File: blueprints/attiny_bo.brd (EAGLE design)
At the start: 36 x 20 mm, 8 parts, among them IC1 ATTiny85, J1 AVR_SPI_PRG_6NS

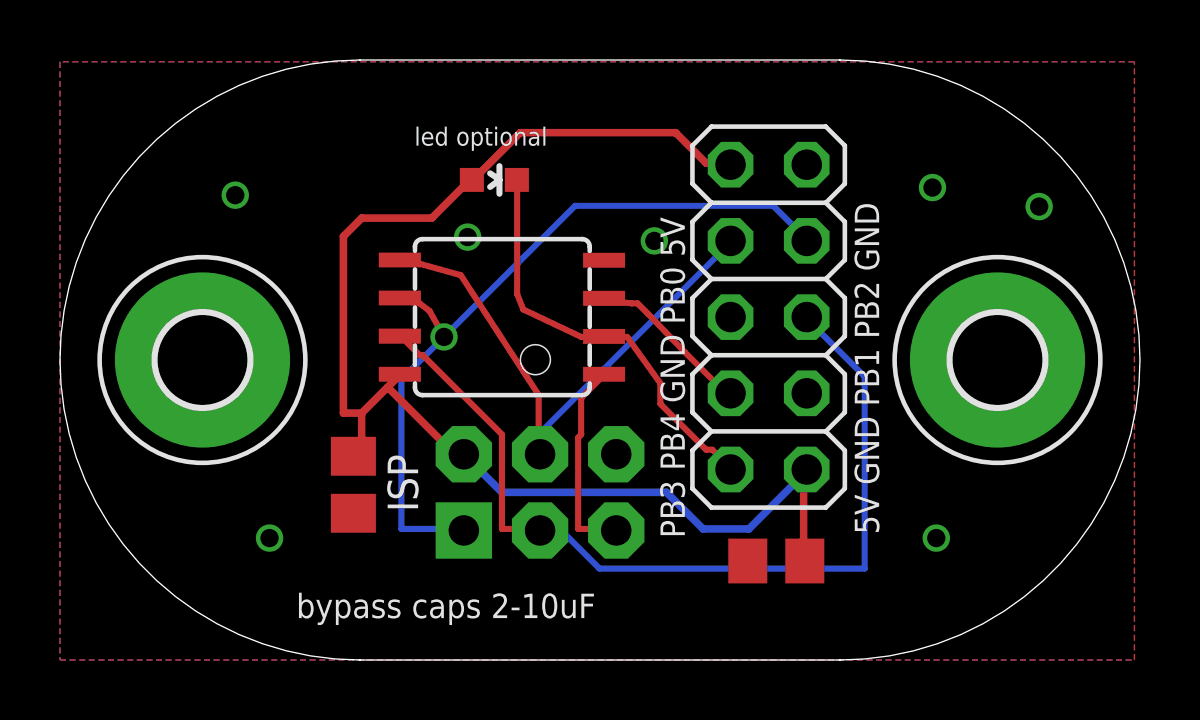
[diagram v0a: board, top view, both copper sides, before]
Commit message: started adding optional crystal to the board
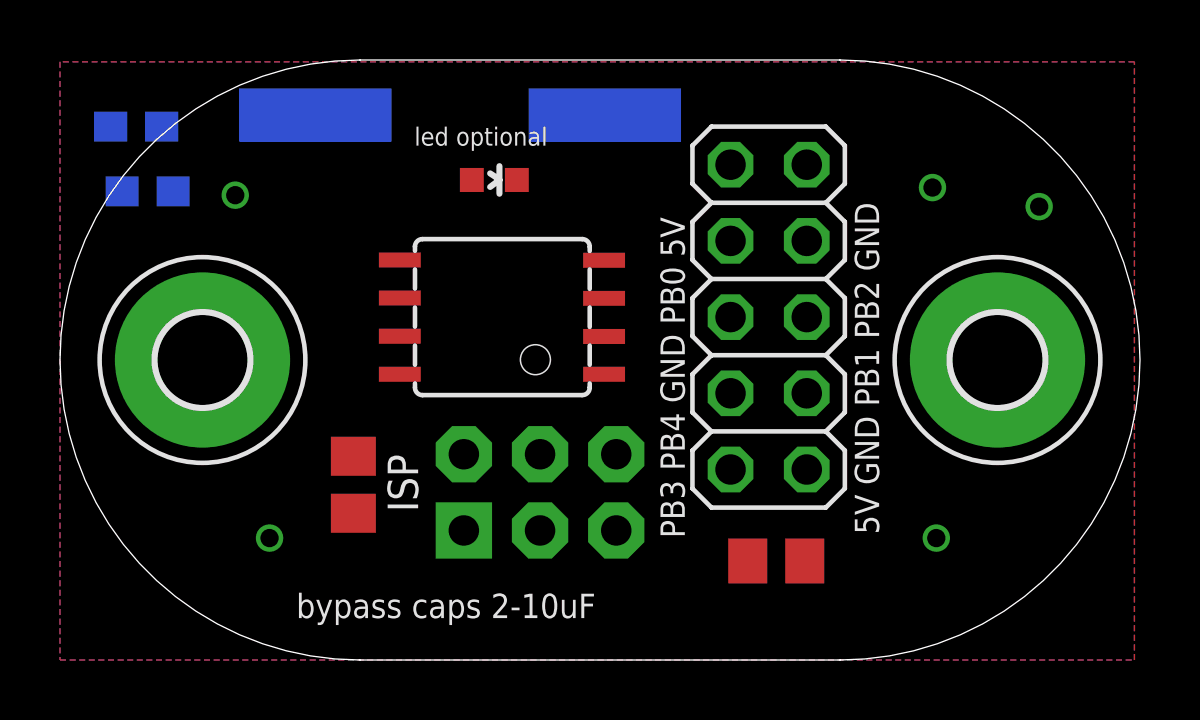
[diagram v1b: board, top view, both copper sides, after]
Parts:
- added C3, C4: (no value), rcl:C0603
- added Q1: (no value), crystal:SM49
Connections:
- net GND: now also C3.1, C4.1
- net PB3: now also C4.2, Q1.1
- net PB4: now also C3.2, Q1.2
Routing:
- net +5V: track 44.7 -> 0.00 mm
- net PB2: track 29.7 -> 0.00 mm
- net PB1: track 25.6 -> 0.00 mm, vias 1 -> 0
- net PB0: track 18.6 -> 0.00 mm
- net PB3: track 13.9 -> 0.00 mm
- net PB5: track 6.80 -> 0.00 mm
- net PB4: track 5.54 -> 0.00 mm

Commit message: started adding optional crystal to the board
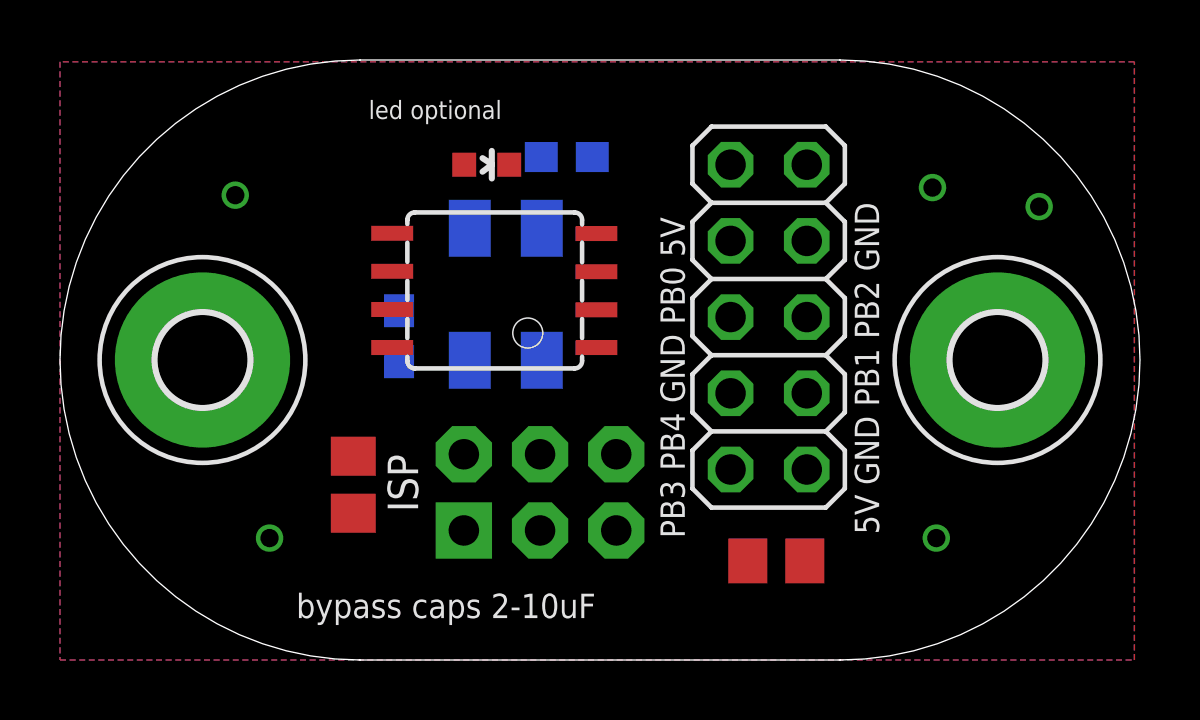
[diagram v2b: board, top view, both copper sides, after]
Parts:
- removed C3, C4: (no value), rcl:C0603
- removed Q1: (no value), crystal:SM49
- added CX0, CX1: 22pF, rcl:C0603
- added XTAL: 16Mhz, crystal:CTS406
- moved IC1 0.92 mm to (14.5, 12.3)
- moved LED1 0.57 mm to (14.2, 16.5)
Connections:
- net GND: now also CX0.1, CX1.1; no longer C3.1, C4.1
- net PB3: now also CX1.2, XTAL.1; no longer C4.2, Q1.1
- net PB4: now also CX0.2, XTAL.3; no longer C3.2, Q1.2
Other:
- board text added: "12pF caps for xtal"
- board text added: "16MHz xtal optional"
- board text removed: "0 & 1 are HW-PWM"
- board text removed: "2,3&4 analog inputs"
- board text removed: "PB5/Reset on ISP pin 5"
- board text removed: "in PBx the x is Arduino pin"

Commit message: optional crystal placed and routed
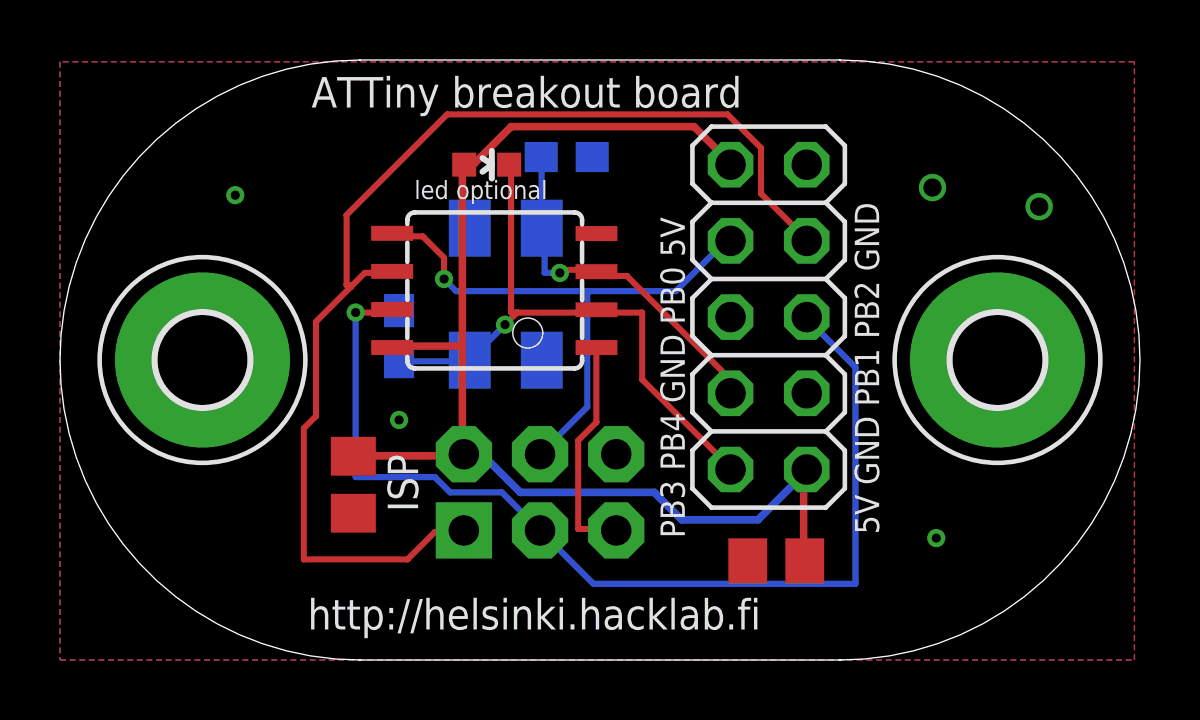
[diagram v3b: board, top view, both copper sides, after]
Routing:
- net +5V: track 0.00 -> 42.0 mm
- net PB1: track 0.00 -> 39.0 mm
- net PB2: track 0.00 -> 34.4 mm, vias 0 -> 1
- net PB3: track 0.00 -> 20.5 mm, vias 0 -> 1
- net PB0: track 0.00 -> 19.3 mm, vias 0 -> 1
- net PB4: track 0.00 -> 12.2 mm, vias 0 -> 1
- net PB5: track 0.00 -> 7.59 mm
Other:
- board text added: "CST406 = SMT 6x3.5"
- board text added: "on top: bypass caps 2-10uF"
- board text removed: "bypass caps 2-10uF"

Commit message: switched to smaller and better available cxtal
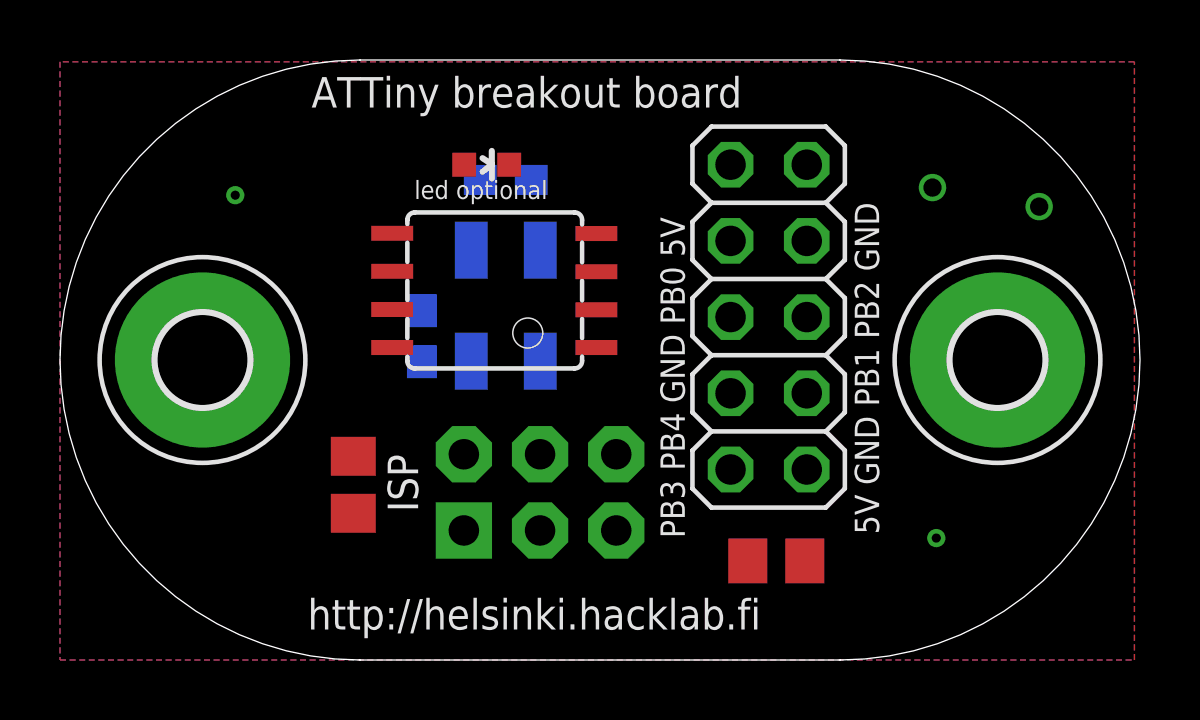
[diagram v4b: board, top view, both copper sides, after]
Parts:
- removed XTAL: 16Mhz, crystal:CTS406
- added Y1: 16MHz, SparkFun-FreqCtrl:CRYSTAL-SMD-5X3
- moved CX0 2.17 mm to (14.9, 16.0), turned to 180 degrees
- moved CX1 0.76 mm to (12.1, 10.8)
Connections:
- net PB3: now also Y1.1; no longer XTAL.1
- net PB4: now also Y1.3; no longer XTAL.3
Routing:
- net +5V: track 42.0 -> 0.00 mm
- net PB1: track 39.0 -> 0.00 mm
- net PB2: track 34.4 -> 0.00 mm, vias 1 -> 0
- net PB3: track 20.5 -> 0.00 mm, vias 1 -> 0
- net PB0: track 19.3 -> 0.00 mm, vias 1 -> 0
- net PB4: track 12.2 -> 0.00 mm, vias 1 -> 0
- net PB5: track 7.59 -> 0.00 mm
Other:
- board text removed: "CST406 = SMT 6x3.5"

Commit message: hand-optimized the routing for the xtal
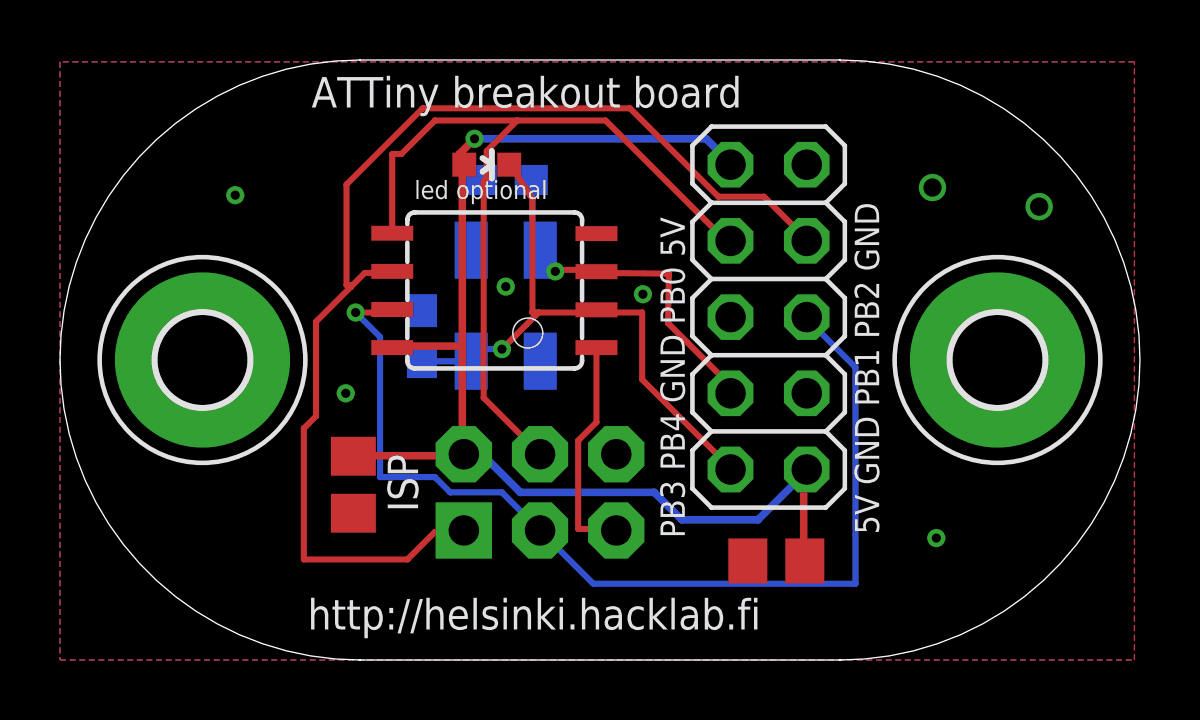
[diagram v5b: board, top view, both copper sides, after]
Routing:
- net +5V: track 0.00 -> 42.1 mm, vias 0 -> 1
- net PB1: track 0.00 -> 38.8 mm
- net PB2: track 0.00 -> 34.0 mm, vias 0 -> 1
- net PB0: track 0.00 -> 28.4 mm
- net PB3: track 0.00 -> 20.0 mm, vias 0 -> 1
- net PB4: track 0.00 -> 12.7 mm, vias 0 -> 1
- net PB5: track 0.00 -> 7.59 mm
